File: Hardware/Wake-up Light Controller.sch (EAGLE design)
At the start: 47 parts, among them IC1 ST1S10, IC2 HT7333, IC3 DS3231/SO, IC4 ATMEGA328P_TQFP, J1 AVR-ISP, J2 Debug, J3 CR1632_3V, Q1 BSS138, Q2 BSS138, Q3 FDN306P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

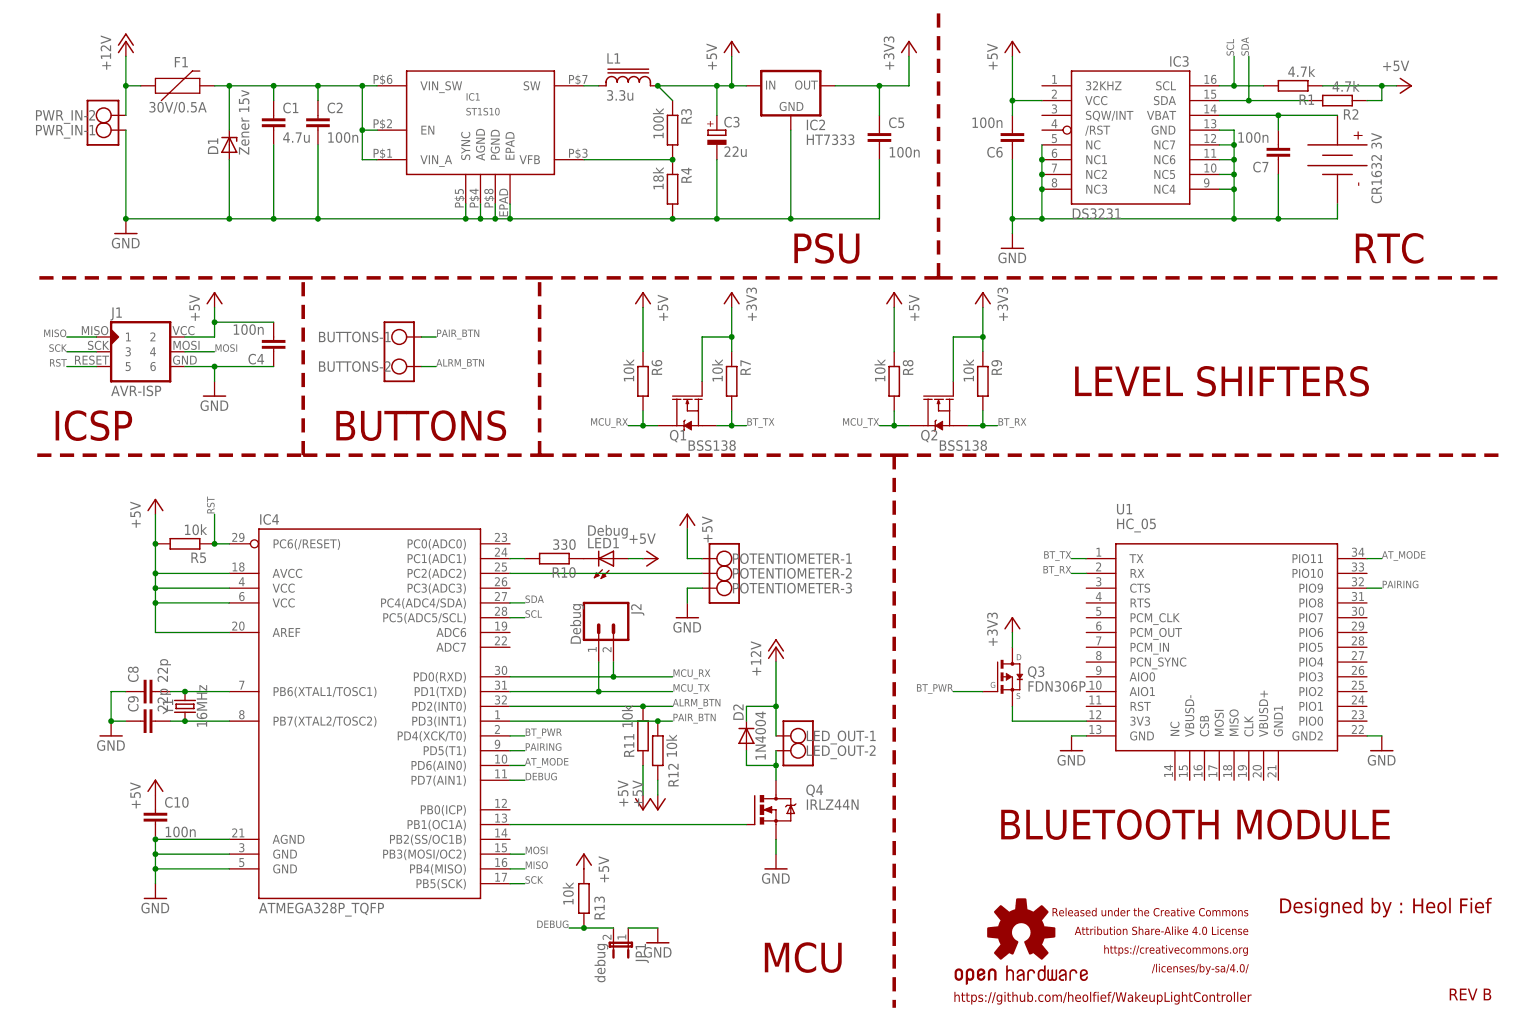
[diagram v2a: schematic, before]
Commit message: Add filtering cap, tweak layout
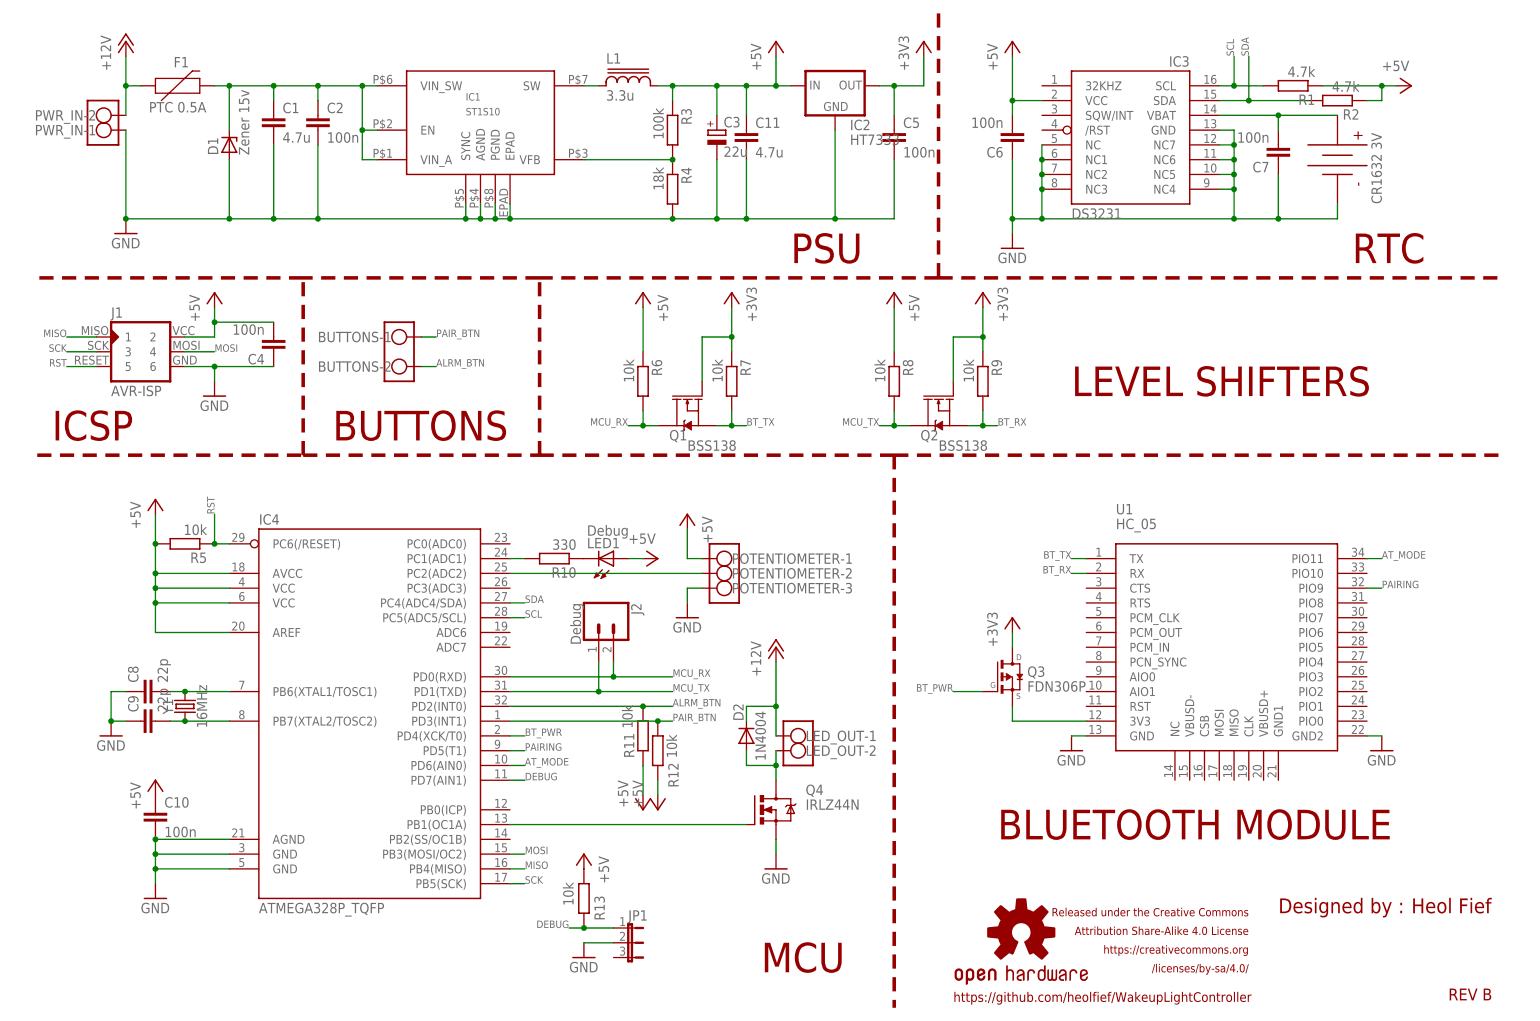
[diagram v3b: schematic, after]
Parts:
- added C11: 4.7u, rcl:C-EUC0805
- F1: value 30V/0.5A -> PTC 0.5A
- JP1: value debug -> (none); device jumper:JP1E -> jumper:JP2E
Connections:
- net +5V: now also C11.1
- net DEBUG: now also JP1.1; no longer JP1.2
- net GND: now also C11.2, JP1.2; no longer JP1.1
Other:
- moved on the sheet: C5, IC2
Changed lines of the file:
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@@
 <?xml version="1.0" encoding="utf-8"?>
 <!DOCTYPE eagle SYSTEM "eagle.dtd">
-<eagle version="8.4.0">
+<eagle version="8.4.1">
 <drawing>
 <settings>
@@
 <part name="P+13" library="supply1" library_urn="urn:adsk.eagle:library:371" deviceset="+5V" device=""/>
 <part name="P+14" library="supply1" library_urn="urn:adsk.eagle:library:371" deviceset="+5V" device=""/>
-<part name="JP1" library="jumper" library_urn="urn:adsk.eagle:library:252" deviceset="JP1E" device="" package3d_urn="urn:adsk.eagle:package:15455/1" value="debug"/>
 <part name="GND10" library="supply1" deviceset="GND" device=""/>
 <part name="R13" library="resistor" library_urn="urn:adsk.eagle:library:348" deviceset="R-EU_" device="M0805" package3d_urn="urn:adsk.eagle:package:26079/1" value="10k"/>
 <part name="P+15" library="supply1" library_urn="urn:adsk.eagle:library:371" deviceset="+5V" device=""/>
-<part name="F1" library="SparkFun-Fuses" library_urn="urn:adsk.eagle:library:517" deviceset="PPTC" device="_PTH" package3d_urn="urn:adsk.eagle:package:38574/1" value="30V/0.5A"/>
+<part name="F1" library="SparkFun-Fuses" library_urn="urn:adsk.eagle:library:517" deviceset="PPTC" device="_PTH" package3d_urn="urn:adsk.eagle:package:38574/1" value="PTC 0.5A"/>
 <part name="D1" library="diode" library_urn="urn:adsk.eagle:library:210" deviceset="ZENER-DIODE" device="SOD80C" package3d_urn="urn:adsk.eagle:package:43405/2" value="Zener 15v"/>
+<part name="C11" library="rcl" deviceset="C-EU" device="C0805" value="4.7u"/>
+<part name="JP1" library="jumper" library_urn="urn:adsk.eagle:library:252" deviceset="JP2E" device="" package3d_urn="urn:adsk.eagle:package:15452/1"/>
 </parts>
 <sheets>
@@
 <instance part="J1" gate="G$1" x="-5.08" y="124.46"/>
 <instance part="GND3" gate="1" x="7.62" y="116.84"/>
-<instance part="IC2" gate="G$1" x="106.68" y="170.18"/>
+<instance part="IC2" gate="G$1" x="114.3" y="170.18"/>
 <instance part="P+6" gate="1" x="-2.54" y="99.06"/>
 <instance part="P+5" gate="1" x="7.62" y="134.62"/>
@@
 <instance part="R3" gate="G$1" x="86.36" y="162.56" rot="R270"/>
 <instance part="L1" gate="G$1" x="78.74" y="170.18"/>
-<instance part="P+2" gate="1" x="96.52" y="177.8"/>
+<instance part="P+2" gate="1" x="104.14" y="177.8"/>
 <instance part="C1" gate="G$1" x="17.78" y="165.1"/>
 <instance part="C2" gate="G$1" x="25.4" y="165.1"/>
-<instance part="+3V31" gate="G$1" x="127" y="177.8"/>
+<instance part="+3V31" gate="G$1" x="129.54" y="177.8"/>
 <instance part="C3" gate="G$1" x="93.98" y="162.56"/>
 <instance part="C4" gate="G$1" x="17.78" y="124.46" rot="R180"/>
-<instance part="C5" gate="G$1" x="121.92" y="162.56"/>
+<instance part="C5" gate="G$1" x="124.46" y="162.56"/>
 <instance part="C10" gate="G$1" x="-2.54" y="45.72"/>
 <instance part="P+9" gate="1" x="-2.54" y="50.8"/>
@@
 <instance part="P+13" gate="1" x="81.28" y="45.72" rot="MR180"/>
 <instance part="P+14" gate="1" x="83.82" y="45.72" rot="MR180"/>
-<instance part="JP1" gate="A" x="78.74" y="22.86" rot="R180"/>
-<instance part="GND10" gate="1" x="83.82" y="22.86"/>
+<instance part="GND10" gate="1" x="71.12" y="20.32"/>
 <instance part="R13" gate="G$1" x="71.12" y="30.48" smashed="yes" rot="R90">
 <attribute name="NAME" x="74.7014" y="26.67" size="1.778" layer="95" rot="R90"/>
@@
 <instance part="F1" gate="G$1" x="0" y="170.18"/>
 <instance part="D1" gate="G$1" x="10.16" y="160.02" rot="R90"/>
+<instance part="C11" gate="G$1" x="99.06" y="162.56"/>
+<instance part="JP1" gate="1" x="78.74" y="22.86" rot="R270"/>
 </instances>
 <busses>
@@
 <wire x1="58.42" y1="147.32" x2="86.36" y2="147.32" width="0.1524" layer="91"/>
 <wire x1="86.36" y1="147.32" x2="93.98" y2="147.32" width="0.1524" layer="91"/>
-<wire x1="93.98" y1="147.32" x2="106.68" y2="147.32" width="0.1524" layer="91"/>
-<wire x1="106.68" y1="147.32" x2="106.68" y2="162.56" width="0.1524" layer="91"/>
+<wire x1="93.98" y1="147.32" x2="99.06" y2="147.32" width="0.1524" layer="91"/>
+<wire x1="99.06" y1="147.32" x2="114.3" y2="147.32" width="0.1524" layer="91"/>
+<wire x1="114.3" y1="147.32" x2="114.3" y2="162.56" width="0.1524" layer="91"/>
 <junction x="58.42" y="147.32"/>
 <pinref part="R4" gate="G$1" pin="2"/>
@@
 <junction x="93.98" y="147.32"/>
 <pinref part="C5" gate="G$1" pin="2"/>
-<wire x1="121.92" y1="157.48" x2="121.92" y2="147.32" width="0.1524" layer="91"/>
-<wire x1="121.92" y1="147.32" x2="106.68" y2="147.32" width="0.1524" layer="91"/>
-<junction x="106.68" y="147.32"/>
+<wire x1="124.46" y1="157.48" x2="124.46" y2="147.32" width="0.1524" layer="91"/>
+<wire x1="124.46" y1="147.32" x2="114.3" y2="147.32" width="0.1524" layer="91"/>
+<junction x="114.3" y="147.32"/>
 <wire x1="53.34" y1="149.86" x2="53.34" y2="147.32" width="0.1524" layer="91"/>
 <junction x="53.34" y="147.32"/>
@@
 <wire x1="10.16" y1="157.48" x2="10.16" y2="147.32" width="0.1524" layer="91"/>
 <junction x="10.16" y="147.32"/>
+<pinref part="C11" gate="G$1" pin="2"/>
+<wire x1="99.06" y1="157.48" x2="99.06" y2="147.32" width="0.1524" layer="91"/>
+<junction x="99.06" y="147.32"/>
 </segment>
 <segment>
@@
 </segment>
 <segment>
-<pinref part="JP1" gate="A" pin="1"/>
+<pinref part="JP1" gate="1" pin="2"/>
 <pinref part="GND10" gate="1" pin="GND"/>
-<wire x1="78.74" y1="25.4" x2="83.82" y2="25.4" width="0.1524" layer="91"/>
+<wire x1="76.2" y1="22.86" x2="71.12" y2="22.86" width="0.1524" layer="91"/>
 </segment>
 </net>
@@
 <pinref part="IC2" gate="G$1" pin="IN"/>
 <pinref part="P+2" gate="1" pin="+5V"/>
-<wire x1="96.52" y1="170.18" x2="96.52" y2="175.26" width="0.1524" layer="91"/>
-<wire x1="96.52" y1="170.18" x2="99.06" y2="170.18" width="0.1524" layer="91"/>
-<junction x="96.52" y="170.18"/>
+<wire x1="104.14" y1="170.18" x2="104.14" y2="175.26" width="0.1524" layer="91"/>
+<wire x1="104.14" y1="170.18" x2="106.68" y2="170.18" width="0.1524" layer="91"/>
+<junction x="104.14" y="170.18"/>
 <pinref part="C3" gate="G$1" pin="+"/>
 <wire x1="93.98" y1="165.1" x2="93.98" y2="170.18" width="0.1524" layer="91"/>
-<wire x1="93.98" y1="170.18" x2="96.52" y2="170.18" width="0.1524" layer="91"/>
+<wire x1="93.98" y1="170.18" x2="99.06" y2="170.18" width="0.1524" layer="91"/>
 <pinref part="L1" gate="G$1" pin="2"/>
 <junction x="93.98" y="170.18"/>
 <pinref part="R3" gate="G$1" pin="1"/>
-<wire x1="83.82" y1="170.18" x2="93.98" y2="170.18" width="0.1524" layer="91"/>
-<wire x1="86.36" y1="167.64" x2="83.82" y2="170.18" width="0.1524" layer="91"/>
-<junction x="83.82" y="170.18"/>
+<wire x1="99.06" y1="170.18" x2="104.14" y2="170.18" width="0.1524" layer="91"/>
+<wire x1="83.82" y1="170.18" x2="86.36" y2="170.18" width="0.1524" layer="91"/>
+<wire x1="86.36" y1="170.18" x2="93.98" y2="170.18" width="0.1524" layer="91"/>
+<wire x1="86.36" y1="167.64" x2="86.36" y2="170.18" width="0.1524" layer="91"/>
+<junction x="86.36" y="170.18"/>
+<pinref part="C11" gate="G$1" pin="1"/>
+<wire x1="99.06" y1="165.1" x2="99.06" y2="170.18" width="0.1524" layer="91"/>
+<junction x="99.06" y="170.18"/>
 </segment>
 <segment>
@@
 <segment>
 <pinref part="IC2" gate="G$1" pin="OUT"/>
-<wire x1="114.3" y1="170.18" x2="121.92" y2="170.18" width="0.1524" layer="91"/>
-<wire x1="121.92" y1="170.18" x2="127" y2="170.18" width="0.1524" layer="91"/>
-<wire x1="127" y1="170.18" x2="127" y2="175.26" width="0.1524" layer="91"/>
+<wire x1="121.92" y1="170.18" x2="124.46" y2="170.18" width="0.1524" layer="91"/>
+<wire x1="124.46" y1="170.18" x2="129.54" y2="170.18" width="0.1524" layer="91"/>
+<wire x1="129.54" y1="170.18" x2="129.54" y2="175.26" width="0.1524" layer="91"/>
 <pinref part="+3V31" gate="G$1" pin="+3V3"/>
 <pinref part="C5" gate="G$1" pin="1"/>
-<wire x1="121.92" y1="165.1" x2="121.92" y2="170.18" width="0.1524" layer="91"/>
-<junction x="121.92" y="170.18"/>
+<wire x1="124.46" y1="165.1" x2="124.46" y2="170.18" width="0.1524" layer="91"/>
+<junction x="124.46" y="170.18"/>
 </segment>
 <segment>
@@
 </segment>
 <segment>
-<pinref part="JP1" gate="A" pin="2"/>
 <wire x1="76.2" y1="25.4" x2="71.12" y2="25.4" width="0.1524" layer="91"/>
 <pinref part="R13" gate="G$1" pin="1"/>
@@
 <junction x="71.12" y="25.4"/>
 <label x="68.58" y="25.4" size="1.27" layer="95" rot="MR0"/>
-</segment>
-</net>
+<pinref part="JP1" gate="1" pin="1"/>
+</segment>
+</net>

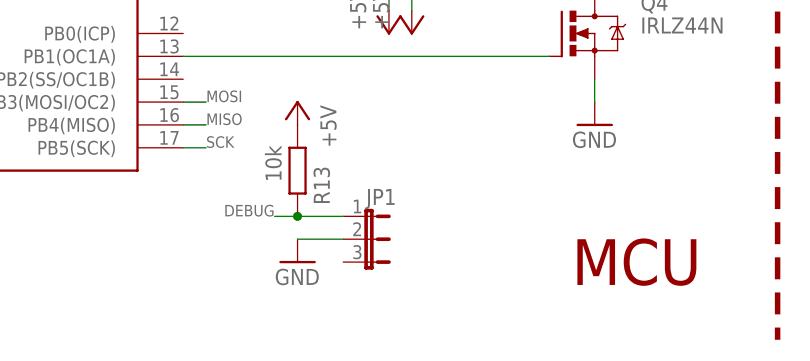
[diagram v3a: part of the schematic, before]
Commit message: Changed component value
Add "debug" value to jumper JP1
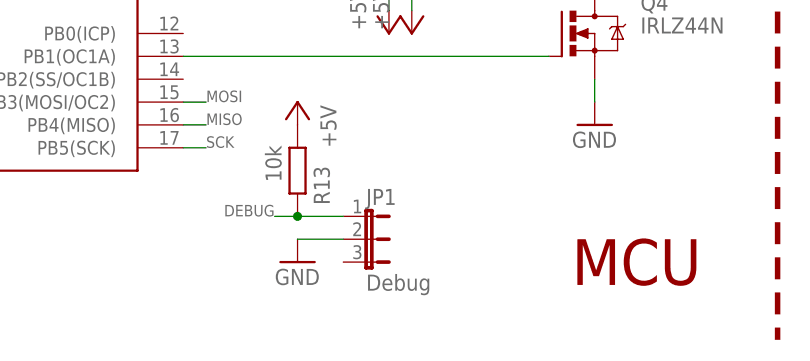
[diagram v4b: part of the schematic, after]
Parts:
- JP1: value (none) -> Debug
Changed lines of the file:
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@@
 <part name="D1" library="diode" library_urn="urn:adsk.eagle:library:210" deviceset="ZENER-DIODE" device="SOD80C" package3d_urn="urn:adsk.eagle:package:43405/2" value="Zener 15v"/>
 <part name="C11" library="rcl" deviceset="C-EU" device="C0805" value="4.7u"/>
-<part name="JP1" library="jumper" library_urn="urn:adsk.eagle:library:252" deviceset="JP2E" device="" package3d_urn="urn:adsk.eagle:package:15452/1"/>
+<part name="JP1" library="jumper" library_urn="urn:adsk.eagle:library:252" deviceset="JP2E" device="" package3d_urn="urn:adsk.eagle:package:15452/1" value="Debug"/>
 </parts>
 <sheets>
